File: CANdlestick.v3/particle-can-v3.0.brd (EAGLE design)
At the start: 29 x 32.3 mm, 13 parts, among them IC1 LM2940, IC2 TJA1049, J1 OBDII

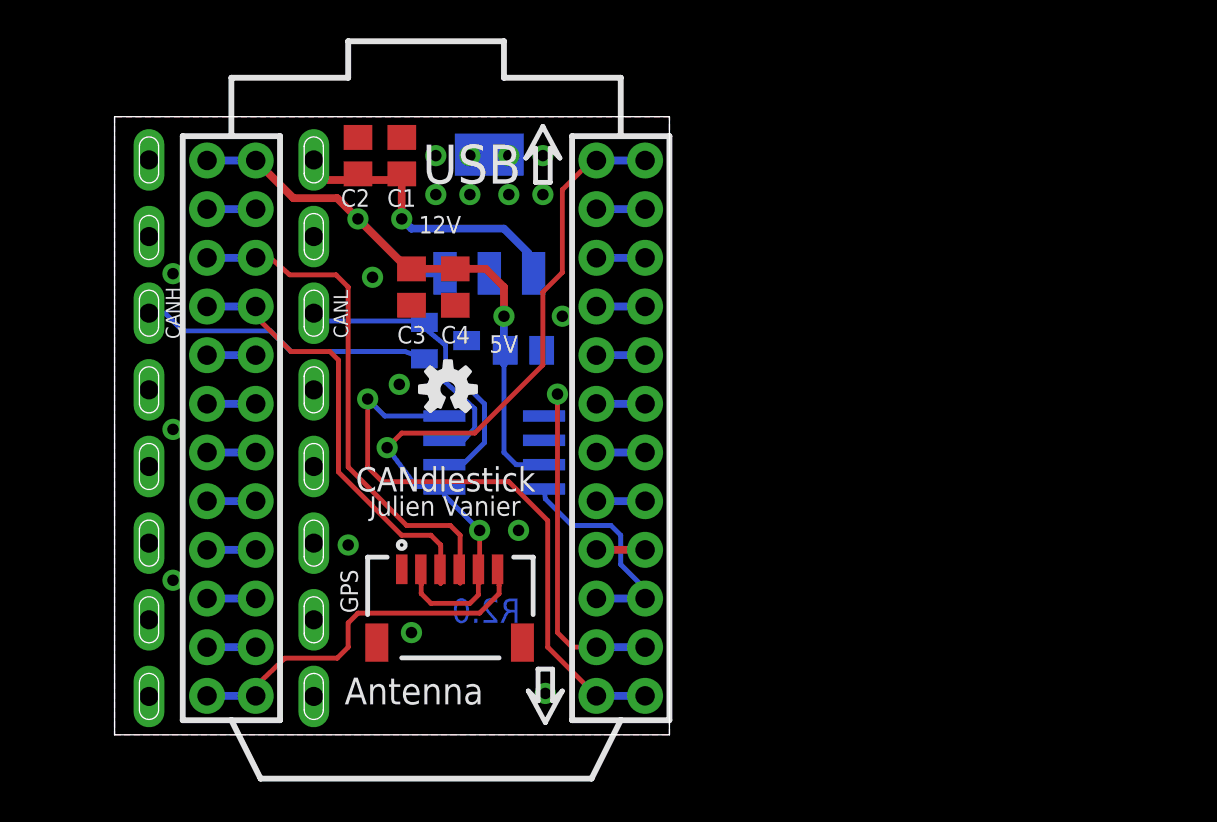
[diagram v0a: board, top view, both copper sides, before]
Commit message: Revision 3 has the PCB extending outward and SD card
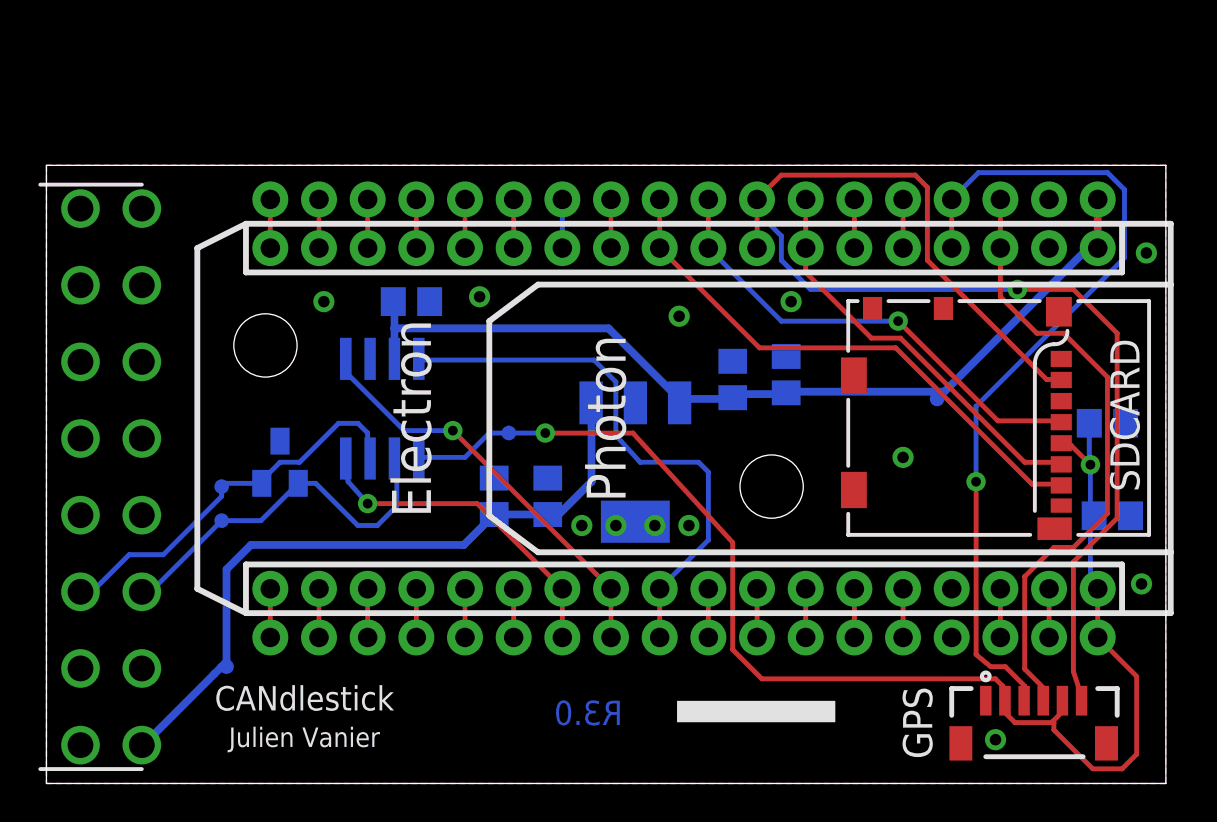
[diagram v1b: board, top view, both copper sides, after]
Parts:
- removed CORE: PHOTONWITH_EXTERNAL_HEADERS, MuniRent:PHOTON_STACKABLE_EXTERNAL
- added C6: 0.1u, rcl:C0805
- added C7: 1u, rcl:C0805
- added ELECTRON: ELECTRON_WITH_EXTERNAL_HEADERS, MuniRent:ELECTRON_EXTERNAL
- added SDCARD: USD-SOCKETMOLEX, MuniRent:MICRO-SD-MOLEX
- added STANDOFF1, STANDOFF2: STAND-OFF, SparkFun-Electromechanical:STAND-OFF
- added TP1: CANH, SparkFun-Passives:PAD.03X.03
- added TP2: CANL, SparkFun-Passives:PAD.03X.03
- added TP3: 12V, SparkFun-Passives:PAD.03X.03
- added TP4: 5V, SparkFun-Passives:PAD.03X.03
- added TP5: 3.3V, SparkFun-Passives:PAD.03X.03
- GPS: value JST_VERTICALHORIZONTAL -> JST; device MuniRent:JST-6-SMD-HOR-1.0MM -> MuniRent:JST-6-SMD-VERT-1.0MM
- J1: device MuniRent:OBDII-STRAIGHT -> MuniRent:OBDII-COMTECH
- moved ZDRAW1 122.0 mm to (-55.2, -52.6)
- moved GPS 31.2 mm to (51.6, 3.05)
- moved F2 22.0 mm to (35.1, 3.68), flipped to the bottom
- moved C3 20.1 mm to (38.6, 21.3), flipped to the bottom, turned to 90 degrees
- moved C1 19.3 mm to (26.2, 15.0), flipped to the bottom
- moved C2 19.1 mm to (23.4, 15.0), flipped to the bottom
- moved C4 15.3 mm to (35.8, 21.1), flipped to the bottom, turned to 90 degrees
- moved IC1 15.0 mm to (30.7, 16.8), turned to 180 degrees
- moved D1 10.7 mm to (12.2, 16.8), turned to 0 degrees
- moved J1 8.27 mm to (1.78, 16.0), flipped to the top
- moved C5 6.37 mm to (19.1, 25.1)
- moved IC2 6.27 mm to (17.5, 19.6), turned to 180 degrees
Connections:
- new net N$1: ELECTRON.13, ELECTRON.@13
- new net N$17: ELECTRON.15, ELECTRON.@15
- new net N$21: ELECTRON.18, ELECTRON.@18
- new net N$22: ELECTRON.19, ELECTRON.@19
- new net N$27: ELECTRON.23, ELECTRON.@23
- new net N$28: ELECTRON.24, ELECTRON.@24
- new net N$29: ELECTRON.22, ELECTRON.@22
- new net N$7: ELECTRON.14, ELECTRON.@14
- new net SD_CS: ELECTRON.10, ELECTRON.@10, SDCARD.2
- new net SPI_MISO: ELECTRON.8, ELECTRON.@8, SDCARD.7
- new net SPI_MOSI: ELECTRON.7, ELECTRON.@7, SDCARD.3
- new net SPI_SCK: ELECTRON.9, ELECTRON.@9, SDCARD.5
- net +12V: now also TP3.P$1
- net 3.3V: now also C6.1, C7.1, ELECTRON.36, ELECTRON.@36, SDCARD.4, TP5.P$1; no longer CORE.24, CORE.@24
- net 5V: now also ELECTRON.1, ELECTRON.@1, TP4.P$1; no longer CORE.1, CORE.@1
- net CANA_EN: now also ELECTRON.25, ELECTRON.@25; no longer CORE.13, CORE.@13
- net CANA_RX: now also ELECTRON.27, ELECTRON.@27; no longer CORE.15, CORE.@15
- net CANA_TX: now also ELECTRON.26, ELECTRON.@26; no longer CORE.14, CORE.@14
- net GND: now also C6.2, C7.2, ELECTRON.2, ELECTRON.33, ELECTRON.@2, ELECTRON.@33, SDCARD.6, SDCARD.CD1, SDCARD.CD2, SDCARD.G1, SDCARD.G2, SDCARD.G3, SDCARD.G4; no longer CORE.2, CORE.21, CORE.@2, CORE.@21
- net GPS_EN: now also ELECTRON.12, ELECTRON.@12; no longer CORE.12, CORE.@12
- net GPS_RX: now also ELECTRON.3, ELECTRON.@3; no longer CORE.3, CORE.@3
- net GPS_TX: now also ELECTRON.4, ELECTRON.@4; no longer CORE.4, CORE.@4
- net HSPD_HI: now also D1.2, TP1.P$1; no longer D1.1
- net HSPD_LO: now also D1.1, TP2.P$1; no longer D1.2
- net N$10: now also ELECTRON.35, ELECTRON.@35; no longer CORE.23, CORE.@23
- net N$11: now also ELECTRON.34, ELECTRON.@34; no longer CORE.22, CORE.@22
- net N$12: now also ELECTRON.32, ELECTRON.@32; no longer CORE.20, CORE.@20
- net N$13: now also ELECTRON.31, ELECTRON.@31; no longer CORE.19, CORE.@19
- net N$14: now also ELECTRON.30, ELECTRON.@30; no longer CORE.18, CORE.@18
- net N$15: now also ELECTRON.29, ELECTRON.@29; no longer CORE.17, CORE.@17
- net N$16: now also ELECTRON.28, ELECTRON.@28; no longer CORE.16, CORE.@16
- net N$18: now also ELECTRON.11, ELECTRON.@11; no longer CORE.11, CORE.@11
- net N$19: now also ELECTRON.16, ELECTRON.@16; no longer CORE.10, CORE.@10
- net N$20: now also ELECTRON.17, ELECTRON.@17; no longer CORE.9, CORE.@9
- net N$23: now also ELECTRON.20, ELECTRON.@20; no longer CORE.8, CORE.@8
- net N$24: now also ELECTRON.21, ELECTRON.@21; no longer CORE.7, CORE.@7
- net N$25: now also ELECTRON.6, ELECTRON.@6; no longer CORE.6, CORE.@6
- net N$26: now also ELECTRON.5, ELECTRON.@5; no longer CORE.5, CORE.@5
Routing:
- net GPS_EN: track 19.7 -> 54.9 mm, vias 0 -> 1
- net 3.3V: track 41.0 -> 73.0 mm
- net SD_CS: track 0.00 -> 28.7 mm
- net SPI_MISO: track 0.00 -> 25.6 mm
- net SPI_SCK: track 0.00 -> 24.8 mm, vias 0 -> 1
- net SPI_MOSI: track 0.00 -> 21.4 mm
- net GPS_TX: track 23.8 -> 43.9 mm, vias 0 -> 1
- net +12V: track 17.7 -> 36.4 mm, vias 1 -> 0
- net CANA_RX: track 11.6 -> 29.0 mm
- net CANA_EN: track 31.2 -> 17.3 mm
- net 5V: track 36.7 -> 48.0 mm, vias 2 -> 0
- net GND: track 5.08 -> 0.00 mm, vias 18 -> 12
- net GPS_RX: track 27.9 -> 32.1 mm
- net CANA_TX: track 18.9 -> 21.8 mm
- net N$29: track 0.00 -> 2.54 mm
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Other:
- board size 29 x 32.3 mm -> 58.4 x 32.3 mm
- board text added: "3.3V"
- board text added: "R3.0"
- board text added: "Revision 3.0"
- board text removed: "Antenna"
- board text removed: "R2.0"
- board text removed: "Revision 2.0"
- board text removed: "USB"

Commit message: Revision 3 grows outward (different form factor)
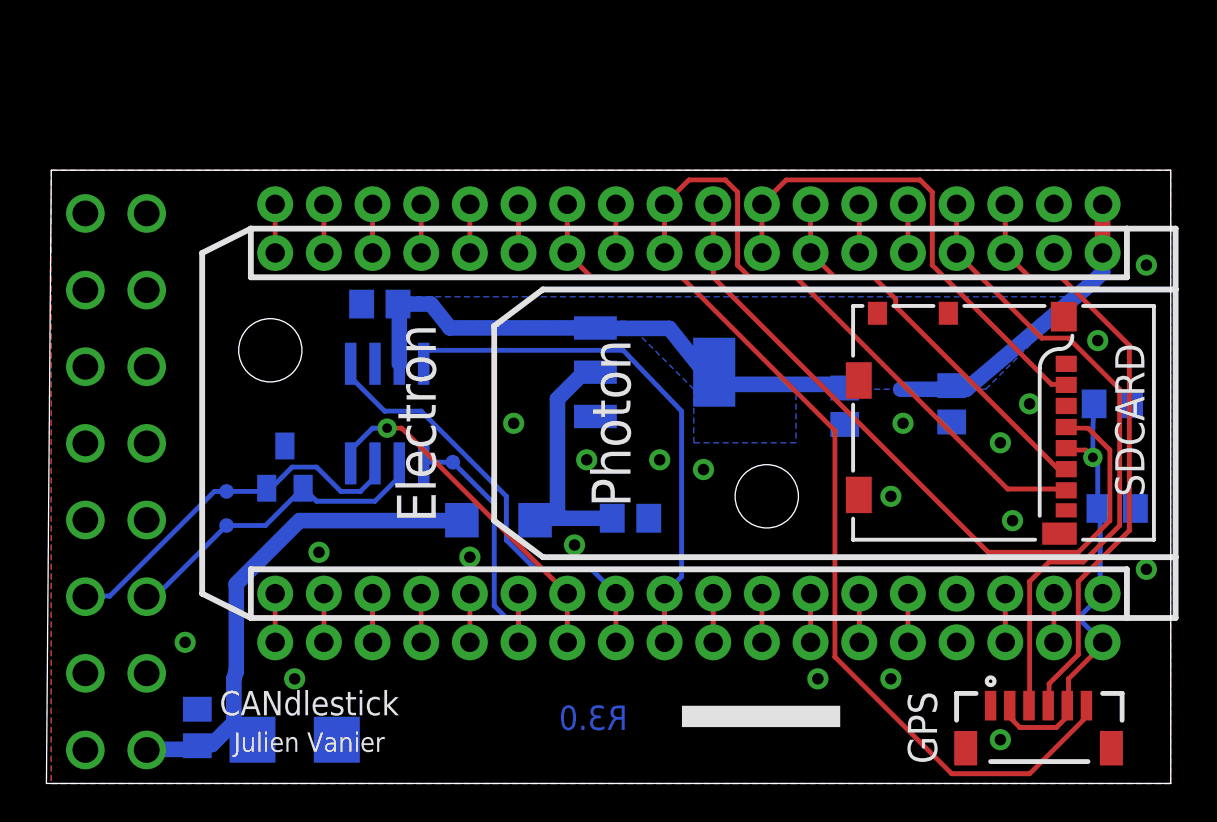
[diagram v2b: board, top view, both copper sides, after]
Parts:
- removed TP4: 5V, SparkFun-Passives:PAD.03X.03
- added D2: 1SMB16CAT3G, BUG:SMB-DIODE
- added D3: RS1J, BUG:SMA-DIODE
- C2: value 0.1u -> 10u
- C4: value 3.3u -> DNP
- IC1: value LM2940 -> NCP1117
- moved C1 21.9 mm to (7.87, 2.92)
- moved C4 11.5 mm to (47.2, 19.8), turned to 270 degrees
- moved C2 7.20 mm to (30.5, 13.8), turned to 180 degrees
- moved IC1 4.81 mm to (31.8, 21.5), turned to 90 degrees
- moved C3 3.47 mm to (41.7, 19.7), turned to 270 degrees
- moved TP5 3.29 mm to (21.2, 16.8)
- moved C5 1.66 mm to (17.4, 25.0), turned to 180 degrees
- moved C7 1.05 mm to (55.6, 19.8)
- moved TP3 0.74 mm to (9.78, 5.46)
- moved STANDOFF2 0.57 mm to (37.6, 15.0)
- moved ZDRAW1 0.57 mm to (-55.7, -52.8)
- moved C6 0.46 mm to (55.9, 14.4)
- moved F2 0.36 mm to (35.4, 3.43)
- moved GPS 0.36 mm to (51.8, 2.79)
- moved IC2 0.36 mm to (17.8, 19.3)
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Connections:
- new net N$31: C2.1, D3.C, IC1.2
- net +12V: now also D2.C, D3.A; no longer C2.1, IC1.1
- net 5V: now also IC1.4; no longer TP4.P$1
- net GND: now also D2.A, IC1.1; no longer IC1.2, IC1.4
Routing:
- net N$31: track 0.00 -> 12.9 mm
- net SPI_SCK: track 24.8 -> 37.6 mm, vias 1 -> 0
- net GPS_TX: track 43.9 -> 33.5 mm, vias 1 -> 0
- net +12V: track 36.4 -> 26.9 mm
- net 3.3V: track 73.0 -> 66.1 mm, vias 2 -> 1
- net GPS_EN: track 54.9 -> 49.7 mm, vias 1 -> 0
- net SD_CS: track 28.7 -> 33.0 mm
- net HSPD_LO: track 19.5 -> 17.0 mm
- net 5V: track 48.0 -> 45.7 mm
- net CANA_TX: track 21.8 -> 23.1 mm, vias 1 -> 0
- net CANA_EN: track 17.3 -> 18.6 mm
- net HSPD_HI: track 20.6 -> 19.5 mm
- net CANA_RX: track 29.0 -> 28.0 mm
- net GPS_RX: track 32.1 -> 31.6 mm
- net SPI_MOSI: track 21.4 -> 20.8 mm
- added copper zone on layer 16, net 5V
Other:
- board size 58.4 x 32.3 mm -> 58.7 x 32 mm

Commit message: Update Readme to show V3 schematics
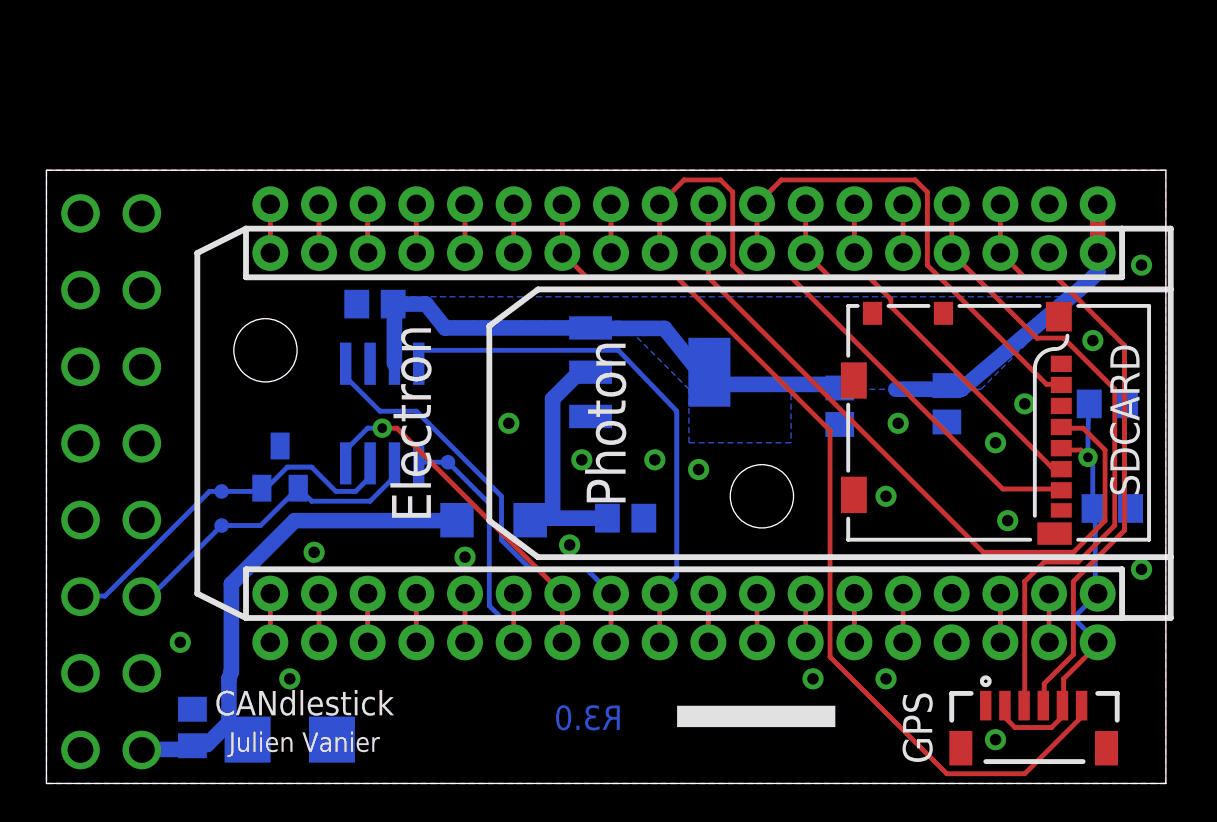
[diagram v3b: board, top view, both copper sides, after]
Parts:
- moved C6 0.25 mm to (55.6, 14.4)
- moved F2 0.25 mm to (35.1, 3.43)
- moved GPS 0.25 mm to (51.6, 2.79)
- moved C2 0.25 mm to (30.2, 13.8)
- moved C5 0.25 mm to (17.1, 25.0)
- moved D2 0.25 mm to (12.7, 2.29)
- moved IC1 0.25 mm to (31.5, 21.5)
- moved IC2 0.25 mm to (17.5, 19.3)
- moved TP5 0.25 mm to (21.0, 16.8)
- moved ELECTRON 0.25 mm to (7.87, 29.0)
- moved J1 0.25 mm to (1.78, 15.7)
- moved C1 0.25 mm to (7.62, 2.92)
- moved D1 0.25 mm to (12.2, 16.5)
- moved STANDOFF1 0.25 mm to (11.4, 22.6)
- moved TP1 0.25 mm to (9.14, 15.2)
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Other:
- board size 58.7 x 32 mm -> 58.4 x 32 mm
